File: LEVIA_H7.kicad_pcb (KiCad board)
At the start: 2 copper layers, 138 parts, among them J1 TF-028-H265, Q1 AO3400A, SW1 SW_Push, U1 USBLC6-2P6, U10 ZX-SH1.0-4PWT, U11 ZX-SH1.0-3PWT, U12 SIT1051TK/3, U13 ZX-SH1.0-4PWT, U14 ICM-42688-P, U15 ICM-42688-P, U16 DPS368XTSA1, U17 IST8310, U18 ZX-SH1.0-4PWT, U19 ZX-SH1.0-6PWT, U2 STM32H743VIHx, U20 ZX-SH1.0-6PWT, U21 ZX-SH1.0-3PWT, U22 ZX-SH1.0-8PWT, U3 ZX-SH1.0-4PWT, U4 LMR43620R5RPER, U5 LMR604303SRAKRQ1, U6 AP7361C-33FGE-7, U7 AP7361C-33FGE-7, U8 ZX-SH1.0-4PWT, U9 AT7456ELAH, Y1 8MHz, Y2 XL2EL89COI-111YLC-27M

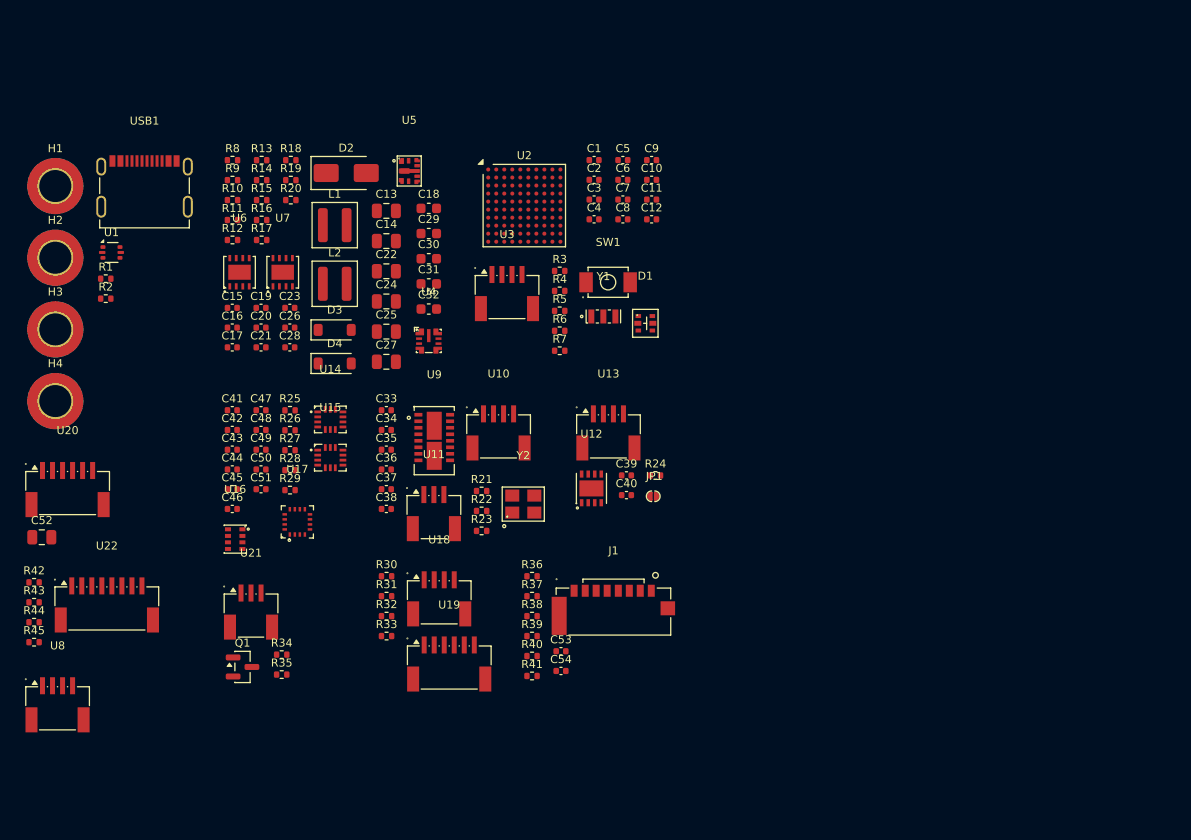
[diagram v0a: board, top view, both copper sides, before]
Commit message: basic psc shape created
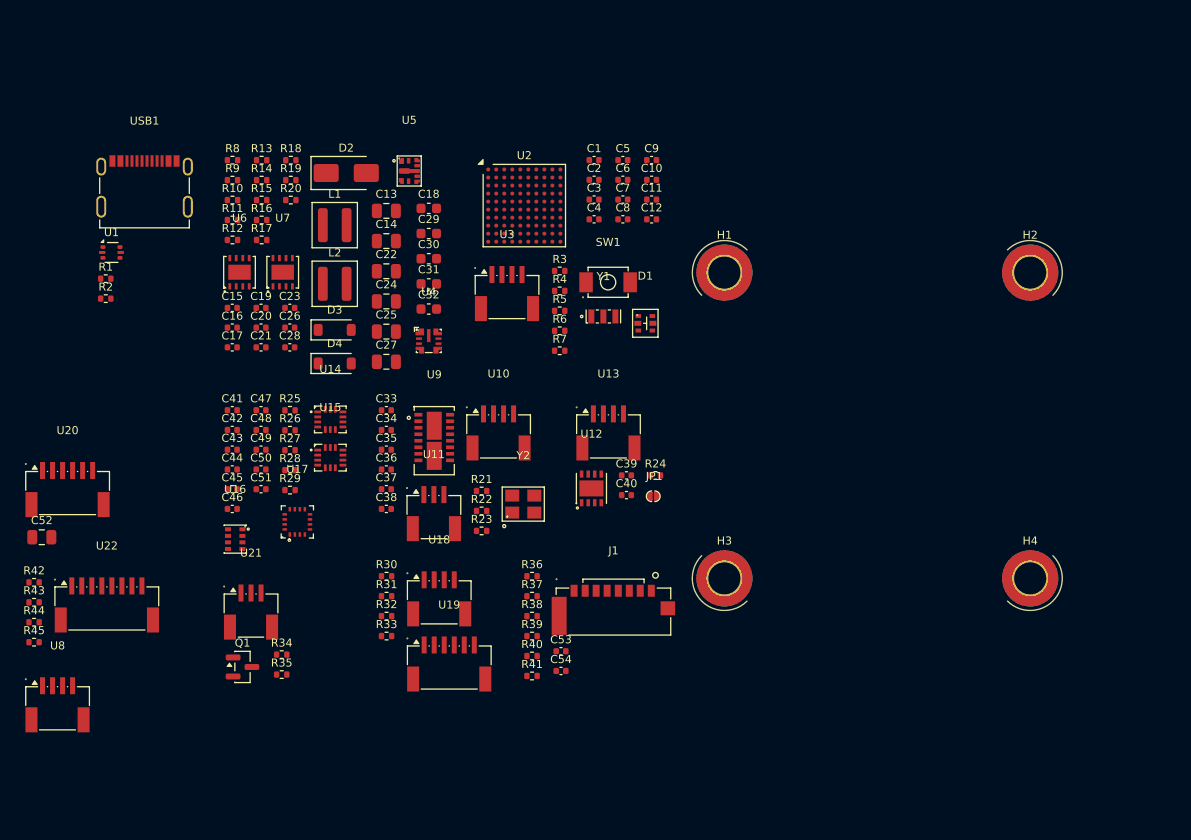
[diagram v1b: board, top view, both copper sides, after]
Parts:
- moved H4 98.8 mm to (174.0, 82.5)
- moved H2 97.3 mm to (174.0, 52.0)
- moved H3 71.2 mm to (143.5, 82.5)
- moved H1 67.3 mm to (143.5, 52.0)
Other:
- board outline added: 36.9 x 36.9 mm
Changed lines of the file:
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@@
 	(footprint "MountingHole:MountingHole_3.2mm_M3_DIN965_Pad_TopBottom"
 		(layer "F.Cu")
-		(at 76.76 43.365)
+		(at 143.5 52)
 		(descr "Mounting Hole 3.2mm, M3, generated by kicad-footprint-generator mountinghole.py")
 		(tags "mountinghole M3 DIN965")
@@
 	(footprint "MountingHole:MountingHole_3.2mm_M3_DIN965_Pad_TopBottom"
 		(layer "F.Cu")
-		(at 76.76 64.815)
+		(at 174 82.5)
 		(descr "Mounting Hole 3.2mm, M3, generated by kicad-footprint-generator mountinghole.py")
 		(tags "mountinghole M3 DIN965")
@@
 	(footprint "MountingHole:MountingHole_3.2mm_M3_DIN965_Pad_TopBottom"
 		(layer "F.Cu")
-		(at 76.76 50.515)
+		(at 174 52)
 		(descr "Mounting Hole 3.2mm, M3, generated by kicad-footprint-generator mountinghole.py")
 		(tags "mountinghole M3 DIN965")
@@
 	(footprint "MountingHole:MountingHole_3.2mm_M3_DIN965_Pad_TopBottom"
 		(layer "F.Cu")
-		(at 76.76 57.665)
+		(at 143.5 82.5)
 		(descr "Mounting Hole 3.2mm, M3, generated by kicad-footprint-generator mountinghole.py")
 		(tags "mountinghole M3 DIN965")
@@
 		)
 	)
+	(gr_arc
+		(start 141.236154 54.263846)
+		(mid 141.236154 49.736154)
+		(end 145.763846 49.736154)
+		(stroke
+			(width 0.05)
+			(type default)
+		)
+		(layer "Edge.Cuts")
+	)
+	(gr_arc
+		(start 145.757566 84.763846)
+		(mid 141.229874 84.763846)
+		(end 141.229874 80.236154)
+		(stroke
+			(width 0.05)
+			(type default)
+		)
+		(layer "Edge.Cuts")
+	)
+	(gr_arc
+		(start 171.736154 49.736154)
+		(mid 176.263846 49.736154)
+		(end 176.263846 54.263846)
+		(stroke
+			(width 0.05)
+			(type default)
+		)
+		(layer "Edge.Cuts")
+	)
+	(gr_arc
+		(start 176.263845 80.236153)
+		(mid 176.263846 84.763845)
+		(end 171.736153 84.763845)
+		(stroke
+			(width 0.05)
+			(type default)
+		)
+		(layer "Edge.Cuts")
+	)
+	(gr_rect
+		(start 143.5 52)
+		(end 174 82.5)
+		(stroke
+			(width 0.1)
+			(type default)
+		)
+		(fill no)
+		(layer "User.4")
+	)
 	(image
 		(at 180.775001 117.925001)
@@
 		)
 	)
+	(dimension
+		(type orthogonal)
+		(layer "User.4")
+		(pts
+			(xy 176.8 52) (xy 176.8 82.5)
+		)
+		(height 3.2)
+		(orientation 1)
+		(format
+			(prefix "")
+			(suffix "")
+			(units 3)
+			(units_format 0)
+			(precision 4)
+			(suppress_zeroes yes)
+		)
+		(style
+			(thickness 0.1)
+			(arrow_length 1.27)
+			(text_position_mode 0)
+			(arrow_direction outward)
+			(extension_height 0.58642)
+			(extension_offset 0.5)
+			(keep_text_aligned yes)
+		)
+		(gr_text "30.5"
+			(at 178.85 67.25 90)
+			(layer "User.4")
+			(effects
+				(font
+					(size 1 1)
+					(thickness 0.15)
+				)
+			)
+		)
+	)
+	(dimension
+		(type orthogonal)
+		(layer "User.4")
+		(pts
+			(xy 143.5 52) (xy 174 52)
+		)
+		(height -6.5)
+		(orientation 0)
+		(format
+			(prefix "")
+			(suffix "")
+			(units 3)
+			(units_format 0)
+			(precision 4)
+			(suppress_zeroes yes)
+		)
+		(style
+			(thickness 0.1)
+			(arrow_length 1.27)
+			(text_position_mode 0)
+			(arrow_direction outward)
+			(extension_height 0.58642)
+			(extension_offset 0.5)
+			(keep_text_aligned yes)
+		)
+		(gr_text "30.5"
+			(at 158.75 44.35 0)
+			(layer "User.4")
+			(effects
+				(font
+					(size 1 1)
+					(thickness 0.15)
+				)
+			)
+		)
+	)
+	(group ""
+		(members "2e379e54-ec8a-486c-b30c-b3b901dbadd1" "3f6889eb-e48f-4aa1-9c44-bff76be4338b"
+			"3ffc9030-9afd-472c-8616-de27ab26e357" "ad2480e9-1147-465e-ba14-c807de98a9d7"
+			"fbacbd19-ef4a-4fb4-80be-980c1486d087"
+		)
+	)

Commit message: grouped ICs and passives
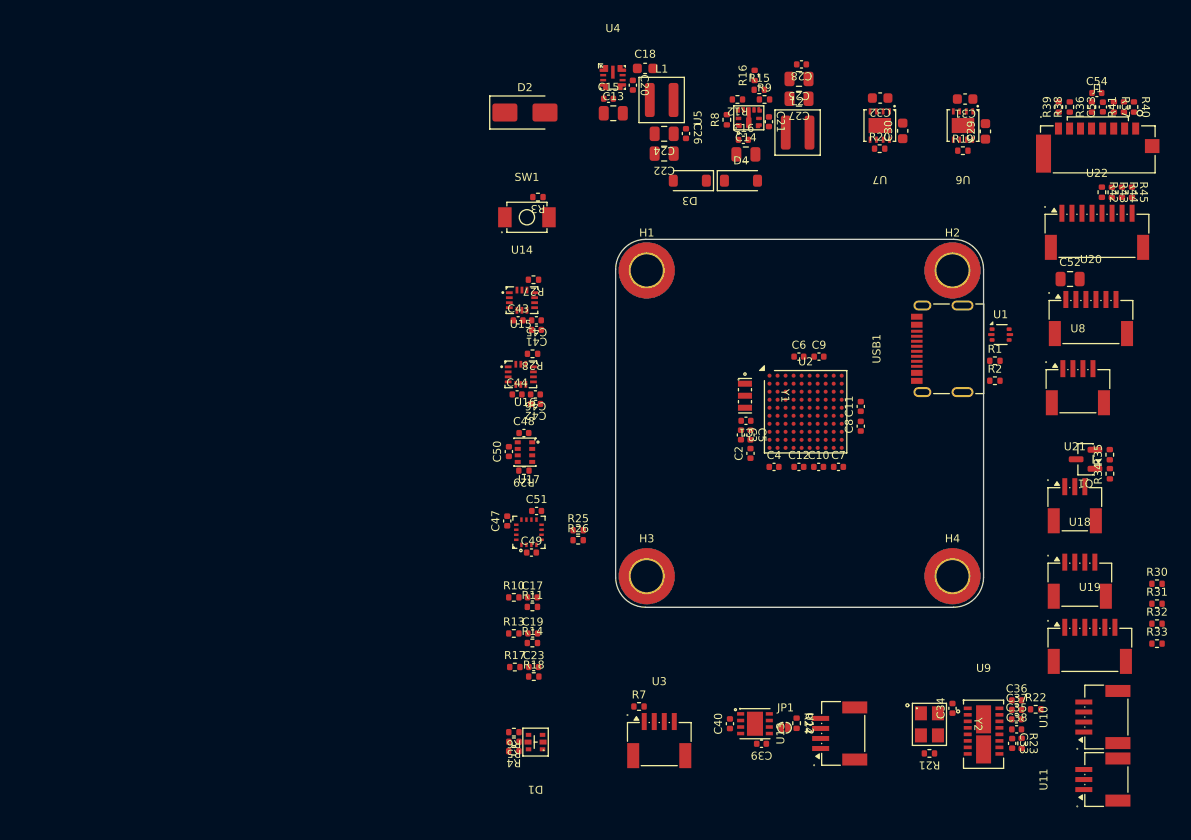
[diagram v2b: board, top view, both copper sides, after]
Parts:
- moved R45 118.4 mm to (184.2, 44.0), turned to -90 degrees
- moved R44 116.7 mm to (183.2, 44.0), turned to -90 degrees
- moved R43 115.0 mm to (182.2, 44.0), turned to -90 degrees
- moved R42 113.4 mm to (181.2, 44.0), turned to -90 degrees
- moved U8 106.6 mm to (178.8, 63.3)
- moved C52 105.8 mm to (178.0, 52.6)
- moved U22 105.5 mm to (180.7, 47.8)
- moved U20 103.5 mm to (180.1, 56.4)
- moved U1 89.1 mm to (171.1, 58.2)
- moved R1 89.1 mm to (170.5, 60.8)
- moved R2 89.1 mm to (170.5, 62.8)
- moved Q1 86.6 mm to (179.5, 70.6), turned to 180 degrees
- moved R35 85.5 mm to (181.9, 70.2), turned to 90 degrees
- moved R34 84.6 mm to (181.9, 72.1), turned to 90 degrees
- moved U21 82.9 mm to (178.4, 75.1)
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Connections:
- C13 pad 1: unconnected-(C13-Pad1) -> VBAT
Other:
- board size 36.9 x 36.9 mm -> 36.7 x 36.7 mm
- board text added: "ADC"
- board text added: "BOOT"
- board text added: "BUZZ"
- board text added: "CAN-FD"
- board text added: "CONNECTORS"
- board text added: "JTAG"
- board text added: "LDOS"
- board text added: "LEDS"
- board text added: "OSD"
- board text added: "SD-CARD"
- board text added: "SENSORS"
- board text added: "SWITCHING REGS"

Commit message: showcase functional blocks on PCB
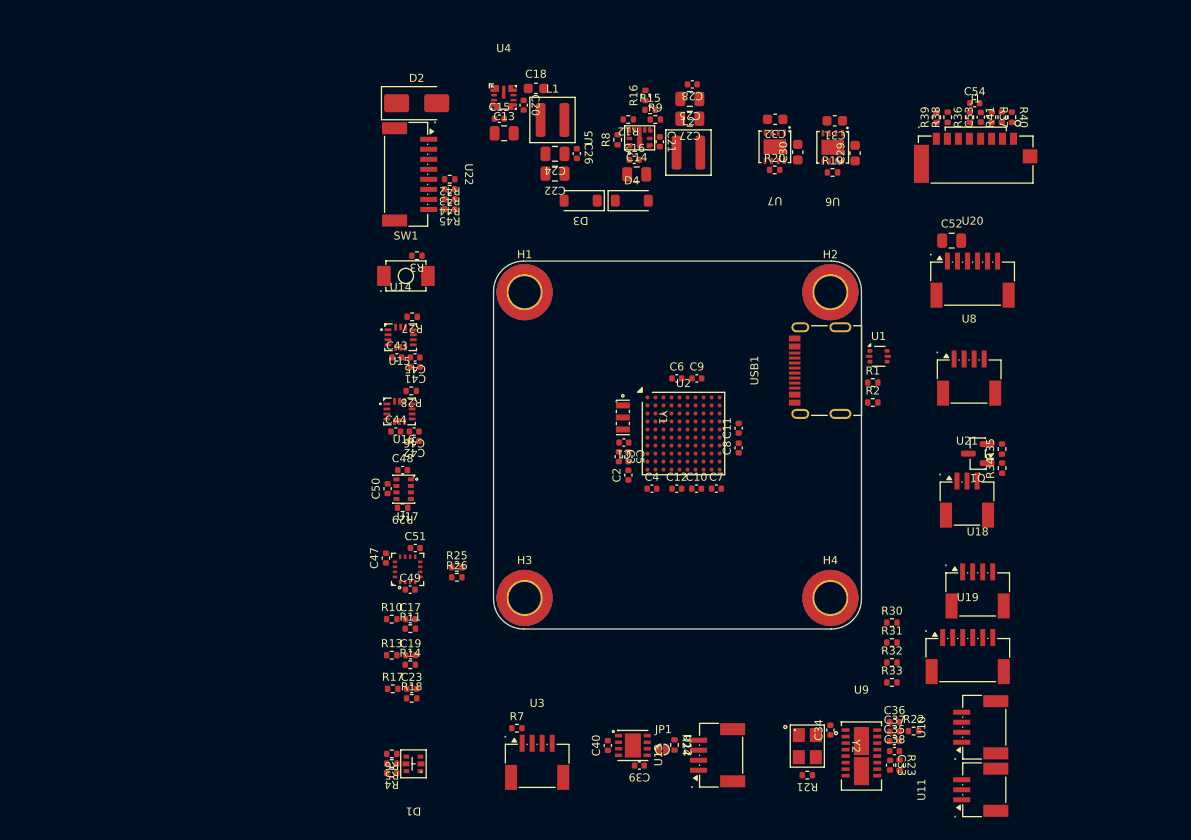
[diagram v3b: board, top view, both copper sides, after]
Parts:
- moved U22 68.6 mm to (112.3, 42.2), turned to -90 degrees
- moved R45 68.1 mm to (116.1, 45.7), turned to 180 degrees
- moved R44 67.1 mm to (116.1, 44.7), turned to 180 degrees
- moved R43 66.1 mm to (116.1, 43.7), turned to 180 degrees
- moved R42 65.1 mm to (116.1, 42.7), turned to 180 degrees
- moved R30 26.7 mm to (160.2, 86.9)
- moved R31 26.7 mm to (160.2, 88.9)
- moved R32 26.7 mm to (160.2, 90.9)
- moved R33 26.7 mm to (160.2, 92.9)
- moved R3 13.4 mm to (112.8, 50.3)
- moved SW1 13.4 mm to (111.7, 52.3)
- moved C29 13.2 mm to (156.5, 40.1)
- moved C31 13.2 mm to (154.5, 36.9)
- moved R19 13.2 mm to (154.3, 42.0)
- moved U6 13.2 mm to (154.3, 39.5)
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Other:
- board text added: "ADCs"
- board text added: "DIGI VTX"
- board text added: "I2C/SPI"
- board text added: "MOTORS"
- board text added: "S E N S O R S"
- board text added: "UARTS"
- board text added: "VTX"
- board text removed: "ADC"
- board text removed: "CONNECTORS"
- board text removed: "SENSORS"

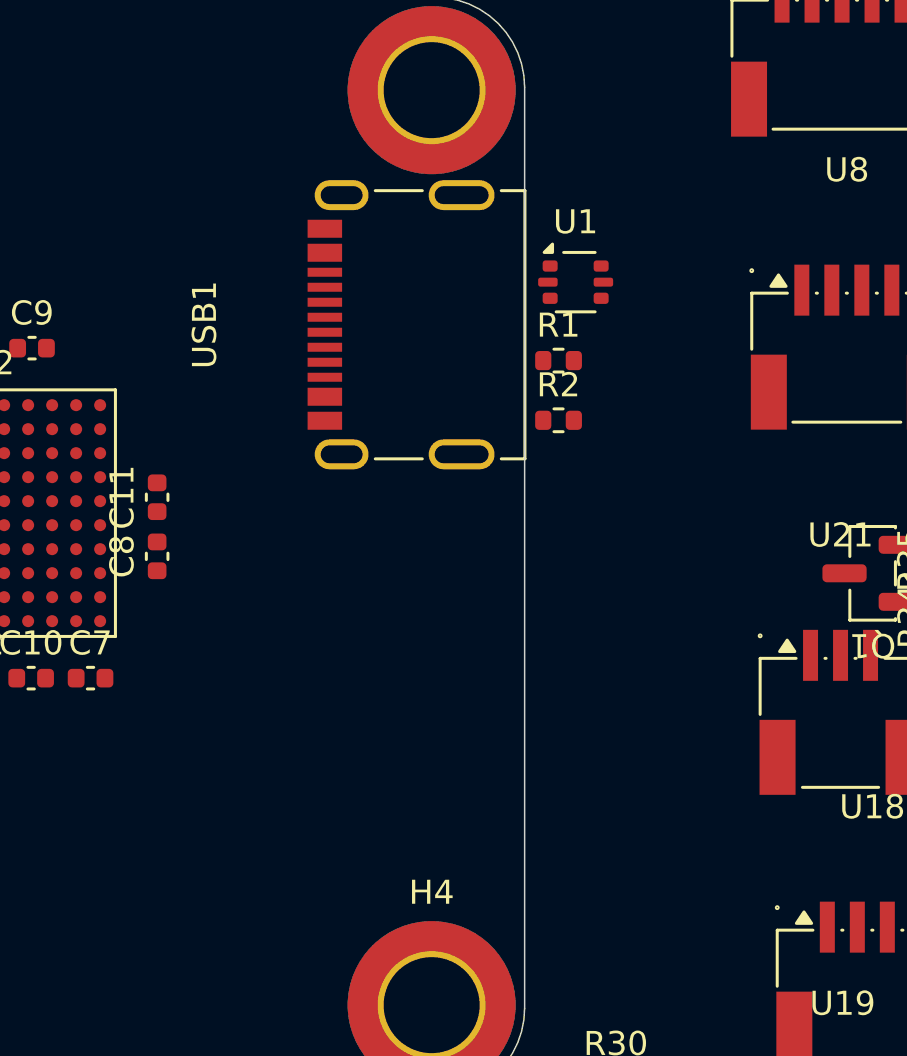
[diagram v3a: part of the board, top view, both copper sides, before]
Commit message: defined stackup
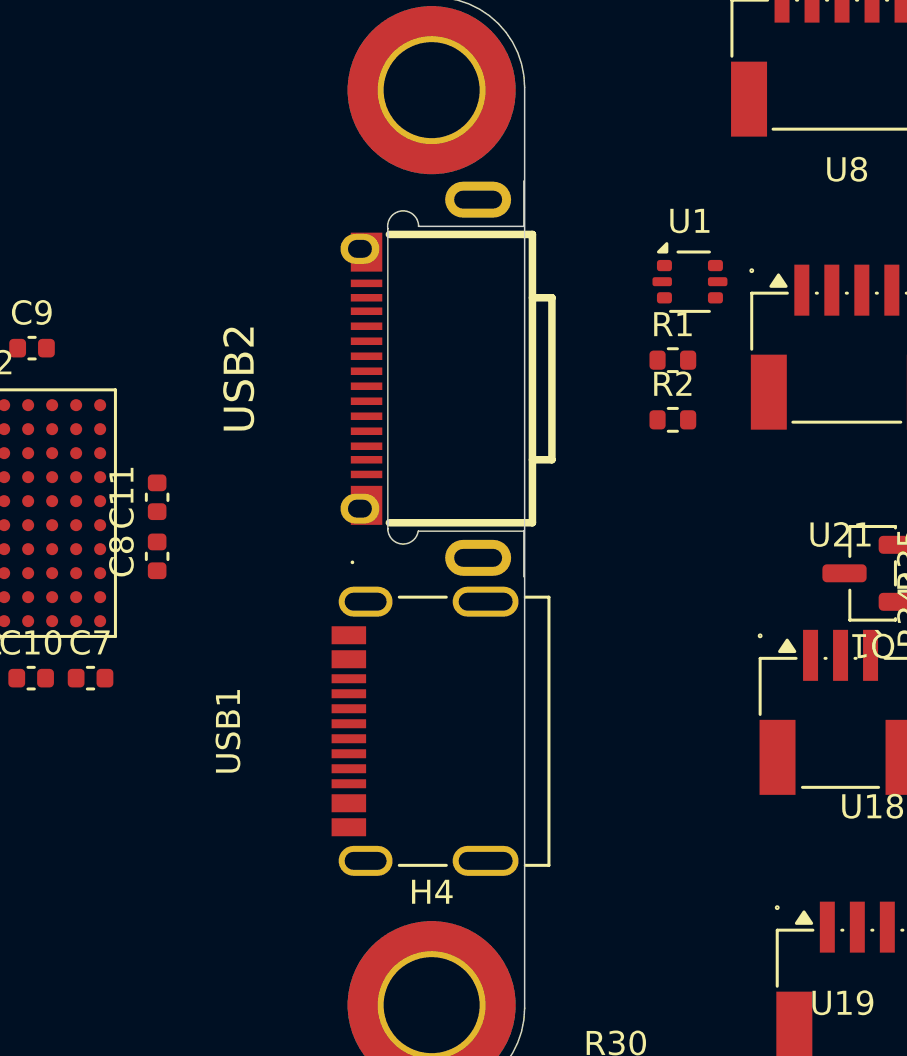
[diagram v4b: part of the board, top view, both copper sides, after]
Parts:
- added USB2: GT-USB-7095C, EasyEDA:USB-C-SMD_GT-USB-7095C, F.Cu at (153.7, 63.6)
- moved USB1 13.6 mm to (153.6, 75.3)
- moved R1 3.81 mm to (162.1, 63.0)
- moved R2 3.81 mm to (162.1, 64.9)
- moved U1 3.81 mm to (162.7, 60.3)
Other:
- copper layers 2 -> 6
